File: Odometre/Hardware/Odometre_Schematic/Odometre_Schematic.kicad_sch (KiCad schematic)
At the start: 35 parts, among them IC1 STM32C092FCP6, J1 Conn_01x03_Pin, J2 Conn_01x03_Pin, J3 Conn_Alim, J4 Conn_Laser1, J5 Conn_Laser2, J6 Conn_01x06_Pin, J7 Conn_01x06_Pin, SW1 Reset_Botton, SW2 Debug_Botton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

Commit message: 5V
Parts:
- J7: footprint Connector_JST:JST_PH_B6B-PH-K_1x06_P2.00mm_Vertical -> Connector_PinHeader_2.54mm:PinHeader_1x03_P2.54mm_Vertical
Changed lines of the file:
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@@
+	)
+	(symbol
+		(lib_id "power:+5V")
+		(at 160.02 78.74 0)
+		(unit 1)
+		(exclude_from_sim no)
+		(in_bom yes)
+		(on_board yes)
+		(dnp no)
+		(fields_autoplaced yes)
+		(property "Reference" "#PWR09"
+			(at 160.02 82.55 0)
+			(effects
+				(font
+					(size 1.27 1.27)
+				)
+				(hide yes)
+			)
+		)
+		(property "Value" "+5V"
+			(at 160.02 73.66 0)
+			(effects
+				(font
+					(size 1.27 1.27)
+				)
+			)
+		)
+		(property "Footprint" ""
+			(at 160.02 78.74 0)
+			(effects
+				(font
+					(size 1.27 1.27)
+				)
+				(hide yes)
+			)
+		)
+		(property "Datasheet" ""
+			(at 160.02 78.74 0)
+			(effects
+				(font
+					(size 1.27 1.27)
+				)
+				(hide yes)
+			)
+		)
+		(property "Description" "Power symbol creates a global label with name \"+5V\""
+			(at 160.02 78.74 0)
+			(effects
+				(font
+					(size 1.27 1.27)
+				)
+				(hide yes)
+			)
+		)
+		(pin "1"
+		)
+		(instances
+			(project ""
+				(path "/3741a7b9-879e-49a1-88bd-82d63456a983"
+					(reference "#PWR09")
+					(unit 1)
+				)
+			)
+		)
 	)
 	(symbol
@@
 			)
 		)
-		(property "Footprint" "Connector_JST:JST_PH_B6B-PH-K_1x06_P2.00mm_Vertical"
+		(property "Footprint" "Connector_PinHeader_2.54mm:PinHeader_1x03_P2.54mm_Vertical"
 			(at 83.82 180.34 0)
 			(effects
@@
 					(unit 1)
 				)
-			)
-		)
-	)
-	(symbol
-		(lib_id "power:+5V")
-		(at 160.02 78.74 0)
-		(unit 1)
-		(exclude_from_sim no)
-		(in_bom yes)
-		(on_board yes)
-		(dnp no)
-		(fields_autoplaced yes)
-		(property "Reference" "#PWR09"
-			(at 160.02 82.55 0)
-			(effects
-				(font
-					(size 1.27 1.27)
-				)
-				(hide yes)
-			)
-		)
-		(property "Value" "+5V"
-			(at 160.02 73.66 0)
-			(effects
-				(font
-					(size 1.27 1.27)
-				)
-			)
-		)
-		(property "Footprint" ""
-			(at 160.02 78.74 0)
-			(effects
-				(font
-					(size 1.27 1.27)
-				)
-				(hide yes)
-			)
-		)
-		(property "Datasheet" ""
-			(at 160.02 78.74 0)
-			(effects
-				(font
-					(size 1.27 1.27)
-				)
-				(hide yes)
-			)
-		)
-		(property "Description" "Power symbol creates a global label with name \"+5V\""
-			(at 160.02 78.74 0)
-			(effects
-				(font
-					(size 1.27 1.27)
-				)
-				(hide yes)
-			)
-		)
-		(pin "1"
-		)
-		(instances
-			(project ""
-				(path "/3741a7b9-879e-49a1-88bd-82d63456a983"
-					(reference "#PWR09")
-					(unit 1)
-				)

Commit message: footprint modifiées
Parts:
- J1, J2: footprint Connector_PinHeader_2.54mm:PinHeader_1x03_P2.54mm_Vertical -> Connector_JST:JST_PH_B3B-PH-K_1x03_P2.00mm_Vertical
- J7: footprint Connector_PinHeader_2.54mm:PinHeader_1x03_P2.54mm_Vertical -> Connector_JST:JST_PH_B6B-PH-K_1x06_P2.00mm_Vertical
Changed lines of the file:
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@@
 			)
 		)
-		(property "Footprint" "Connector_PinHeader_2.54mm:PinHeader_1x03_P2.54mm_Vertical"
+		(property "Footprint" "Connector_JST:JST_PH_B3B-PH-K_1x03_P2.00mm_Vertical"
 			(at 99.06 149.86 0)
 			(effects
@@
 			)
 		)
-		(property "Footprint" "Connector_PinHeader_2.54mm:PinHeader_1x03_P2.54mm_Vertical"
+		(property "Footprint" "Connector_JST:JST_PH_B3B-PH-K_1x03_P2.00mm_Vertical"
 			(at 99.06 133.35 0)
 			(effects
@@
 			)
 		)
-		(property "Footprint" "Connector_PinHeader_2.54mm:PinHeader_1x03_P2.54mm_Vertical"
+		(property "Footprint" "Connector_JST:JST_PH_B6B-PH-K_1x06_P2.00mm_Vertical"
 			(at 83.82 180.34 0)
 			(effects

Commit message: import empreintes
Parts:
- removed SW1: Reset_Botton, Button_Switch_THT:SW_PUSH_6mm, symbol Switch:SW_Push
- removed SW2: Debug_Botton, Button_Switch_THT:SW_PUSH_6mm, symbol Switch:SW_Push
- added S1, S2: 430182043816, 430182043816:430182043816, symbol 430182043816:430182043816
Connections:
- net D_Botton: now also S2.1
- net GND: now also S1.4, S2.4
- net NRST: now also S1.1
- no-connect marks 11 -> 15

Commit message: import empreinte
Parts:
- S1, S2: footprint 430182043816:430182043816 -> projo:430182043816
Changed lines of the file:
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@@
 			)
 		)
-		(property "Footprint" "430182043816:430182043816"
+		(property "Footprint" "projo:430182043816"
 			(at 259.08 87.63 0)
 			(effects
@@
 			)
 		)
-		(property "Footprint" "430182043816:430182043816"
+		(property "Footprint" "projo:430182043816"
 			(at 259.08 109.22 0)
 			(effects

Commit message: modif empreintes
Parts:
- J4, J5: footprint Connector_PinSocket_2.54mm:PinSocket_1x02_P2.54mm_Vertical -> Connector_PinHeader_2.54mm:PinHeader_1x03_P2.54mm_Vertical
- J6: footprint Connector_PinHeader_2.54mm:PinHeader_1x03_P2.54mm_Vertical -> Connector_PinHeader_2.54mm:PinHeader_1x06_P2.54mm_Vertical
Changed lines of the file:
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@@
 			)
 		)
-		(property "Footprint" "Connector_PinSocket_2.54mm:PinSocket_1x02_P2.54mm_Vertical"
+		(property "Footprint" "Connector_PinHeader_2.54mm:PinHeader_1x03_P2.54mm_Vertical"
 			(at 36.83 172.72 0)
 			(effects
@@
 			)
 		)
-		(property "Footprint" "Connector_PinSocket_2.54mm:PinSocket_1x02_P2.54mm_Vertical"
+		(property "Footprint" "Connector_PinHeader_2.54mm:PinHeader_1x03_P2.54mm_Vertical"
 			(at 36.83 185.42 0)
 			(effects
@@
 			)
 		)
-		(property "Footprint" "Connector_PinHeader_2.54mm:PinHeader_1x03_P2.54mm_Vertical"
+		(property "Footprint" "Connector_PinHeader_2.54mm:PinHeader_1x06_P2.54mm_Vertical"
 			(at 39.37 137.16 0)
 			(effects

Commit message: modifs che pas
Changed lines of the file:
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@@
 	)
 	(junction
+		(at 120.65 31.75)
+		(diameter 0)
+		(color 0 0 0 0)
+	)
+	(junction
 		(at 120.65 78.74)
 		(diameter 0)
@@
 	)
 	(junction
-		(at 120.65 31.75)
+		(at 128.27 31.75)
 		(diameter 0)
 		(color 0 0 0 0)
@@
 	(wire
 		(pts
+			(xy 128.27 31.75) (xy 133.35 31.75)
+		)
+		(stroke
+			(width 0)
+			(type default)
+		)
+	)
+	(wire
+		(pts
 			(xy 74.93 78.74) (xy 74.93 81.28)
 		)
@@
 	(wire
 		(pts
-			(xy 120.65 31.75) (xy 133.35 31.75)
-		)
-		(stroke
-			(width 0)
-			(type default)
-		)
-	)
-	(wire
-		(pts
 			(xy 261.62 93.98) (xy 270.51 93.98)
 		)
@@
 	(wire
 		(pts
+			(xy 120.65 31.75) (xy 128.27 31.75)
+		)
+		(stroke
+			(width 0)
+			(type default)
+		)
+	)
+	(wire
+		(pts
 			(xy 252.73 54.61) (xy 256.54 54.61)
 		)
@@
 					(unit 1)
 				)
+			)
+		)
+	)
+	(symbol
+		(lib_id "power:PWR_FLAG")
+		(at 128.27 31.75 0)
+		(unit 1)
+		(exclude_from_sim no)
+		(in_bom yes)
+		(on_board yes)
+		(dnp no)
+		(fields_autoplaced yes)
+		(property "Reference" "#FLG01"
+			(at 128.27 29.845 0)
+			(effects
+				(font
+					(size 1.27 1.27)
+				)
+				(hide yes)
+			)
+		)
+		(property "Value" "PWR_FLAG"
+			(at 128.27 26.67 0)
+			(effects
+				(font
+					(size 1.27 1.27)
+				)
+			)
+		)
+		(property "Footprint" ""
+			(at 128.27 31.75 0)
+			(effects
+				(font
+					(size 1.27 1.27)
+				)
+				(hide yes)
+			)
+		)
+		(property "Datasheet" "~"
+			(at 128.27 31.75 0)
+			(effects
+				(font
+					(size 1.27 1.27)
+				)
+				(hide yes)
+			)
+		)
+		(property "Description" "Special symbol for telling ERC where power comes from"
+			(at 128.27 31.75 0)
+			(effects
+				(font
+					(size 1.27 1.27)
+				)
+				(hide yes)
+			)
+		)
+		(pin "1"
+		)
+		(instances
+			(project ""
+				(path "/3741a7b9-879e-49a1-88bd-82d63456a983"
+					(reference "#FLG01")
+					(unit 1)
+				)

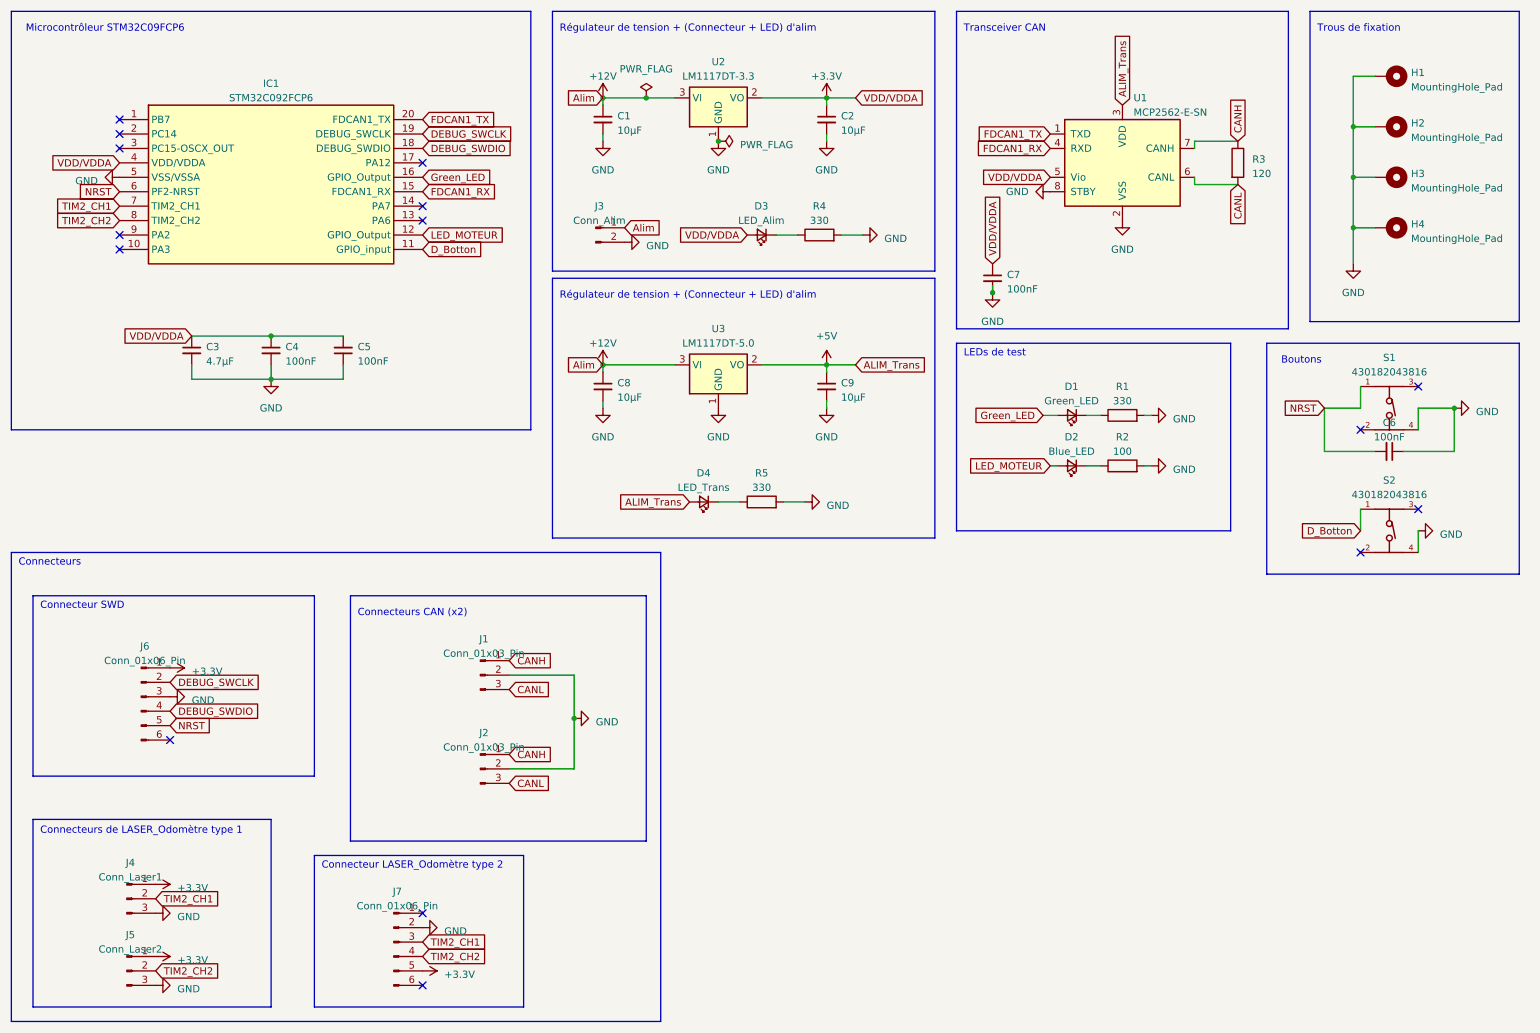
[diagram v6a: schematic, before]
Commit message: routage du pcb
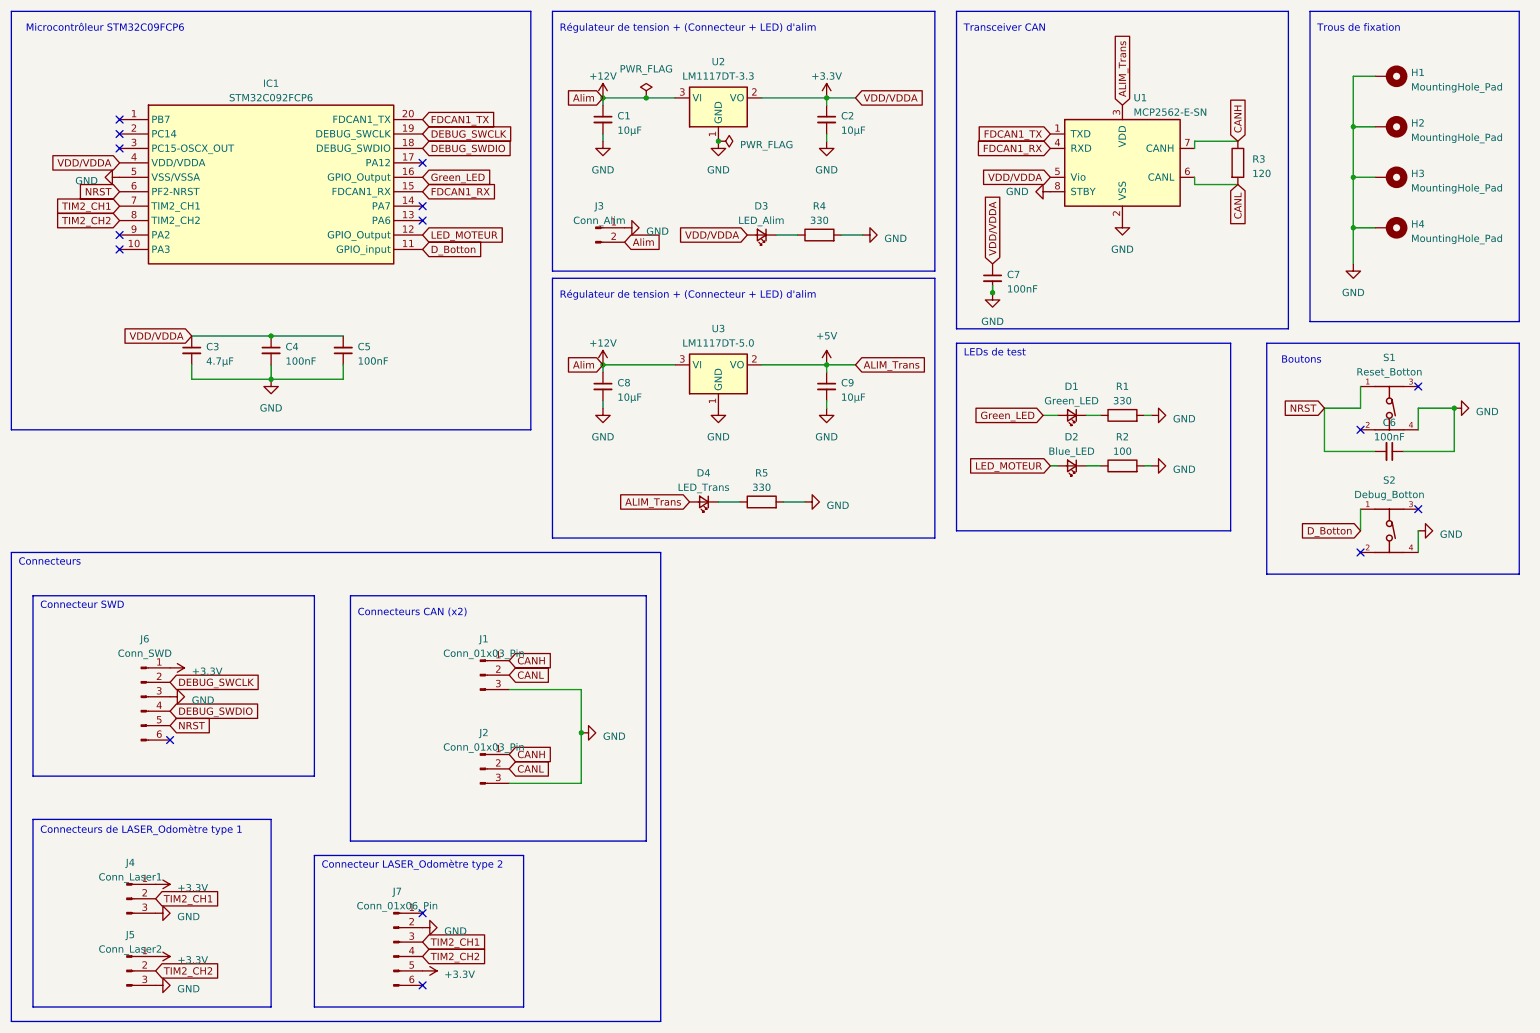
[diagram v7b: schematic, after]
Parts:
- J6: value Conn_01x06_Pin -> Conn_SWD
- S1: value 430182043816 -> Reset_Botton
- S2: value 430182043816 -> Debug_Botton
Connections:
- net +12V: now also J3.2 (Pin_2); no longer J3.1 (Pin_1)
- net CANL: now also J1.2 (Pin_2), J2.2 (Pin_2); no longer J1.3 (Pin_3), J2.3 (Pin_3)
- net GND: now also J1.3 (Pin_3), J2.3 (Pin_3), J3.1 (Pin_1); no longer J1.2 (Pin_2), J2.2 (Pin_2), J3.2 (Pin_2)
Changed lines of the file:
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@@
 	)
 	(junction
-		(at 115.57 140.97)
+		(at 116.84 143.51)
 		(diameter 0)
 		(color 0 0 0 0)
@@
 	(wire
 		(pts
-			(xy 115.57 149.86) (xy 104.14 149.86)
-		)
-		(stroke
-			(width 0)
-			(type default)
-		)
-	)
-	(wire
-		(pts
 			(xy 256.54 27.94) (xy 252.73 27.94)
 		)
@@
 	(wire
 		(pts
-			(xy 115.57 140.97) (xy 115.57 149.86)
+			(xy 116.84 143.51) (xy 116.84 152.4)
 		)
 		(stroke
@@
 	(wire
 		(pts
+			(xy 104.14 135.89) (xy 116.84 135.89)
+		)
+		(stroke
+			(width 0)
+			(type default)
+		)
+	)
+	(wire
+		(pts
 			(xy 120.65 31.75) (xy 120.65 33.02)
 		)
@@
 	(wire
 		(pts
+			(xy 104.14 152.4) (xy 116.84 152.4)
+		)
+		(stroke
+			(width 0)
+			(type default)
+		)
+	)
+	(wire
+		(pts
 			(xy 160.02 86.36) (xy 160.02 85.09)
 		)
@@
 	(wire
 		(pts
-			(xy 115.57 133.35) (xy 115.57 140.97)
+			(xy 116.84 135.89) (xy 116.84 143.51)
 		)
 		(stroke
@@
 	(wire
 		(pts
-			(xy 104.14 133.35) (xy 115.57 133.35)
-		)
-		(stroke
-			(width 0)
-			(type default)
-		)
-	)
-	(wire
-		(pts
 			(xy 162.56 55.88) (xy 166.37 55.88)
 		)
@@
 	(global_label "Alim"
 		(shape input)
-		(at 124.46 54.61 0)
+		(at 124.46 57.15 0)
 		(fields_autoplaced yes)
 		(effects
@@
 		)
 		(property "Intersheetrefs" "${INTERSHEET_REFS}"
-			(at 131.4177 54.61 0)
+			(at 131.4177 57.15 0)
 			(effects
 				(font
@@
 	(global_label "CANL"
 		(shape input)
-		(at 104.14 152.4 0)
+		(at 104.14 149.86 0)
 		(fields_autoplaced yes)
 		(effects
@@
 		)
 		(property "Intersheetrefs" "${INTERSHEET_REFS}"
-			(at 111.763 152.4 0)
+			(at 111.763 149.86 0)
 			(effects
 				(font
@@
 	(global_label "CANL"
 		(shape input)
-		(at 104.14 135.89 0)
+		(at 104.14 133.35 0)
 		(fields_autoplaced yes)
 		(effects
@@
 		)
 		(property "Intersheetrefs" "${INTERSHEET_REFS}"
-			(at 111.763 135.89 0)
+			(at 111.763 133.35 0)
 			(effects
 				(font
@@
 			)
 		)
-		(property "Value" "430182043816"
+		(property "Value" "Reset_Botton"
 			(at 259.08 80.01 0)
 			(effects
@@
 			)
 		)
-		(property "Value" "430182043816"
+		(property "Value" "Debug_Botton"
 			(at 259.08 101.6 0)
 			(effects
@@
 	(symbol
 		(lib_id "power:GND")
-		(at 115.57 140.97 90)
+		(at 116.84 143.51 90)
 		(unit 1)
 		(exclude_from_sim no)
@@
 		(fields_autoplaced yes)
 		(property "Reference" "#PWR022"
-			(at 121.92 140.97 0)
+			(at 123.19 143.51 0)
 			(effects
 				(font
@@
 		)
 		(property "Value" "GND"
-			(at 119.38 141.605 90)
+			(at 120.65 144.145 90)
 			(effects
 				(font
@@
 		)
 		(property "Footprint" ""
-			(at 115.57 140.97 0)
+			(at 116.84 143.51 0)
 			(effects
 				(font
@@
 		)
 		(property "Datasheet" ""
-			(at 115.57 140.97 0)
+			(at 116.84 143.51 0)
 			(effects
 				(font
@@
 		)
 		(property "Description" ""
-			(at 115.57 140.97 0)
+			(at 116.84 143.51 0)
 			(effects
 				(font
@@
 	(symbol
 		(lib_id "power:GND")
-		(at 124.46 57.15 90)
+		(at 124.46 54.61 90)
 		(unit 1)
 		(exclude_from_sim no)
@@
 		(fields_autoplaced yes)
 		(property "Reference" "#PWR019"
-			(at 130.81 57.15 0)
+			(at 130.81 54.61 0)
 			(effects
 				(font
@@
 		)
 		(property "Value" "GND"
-			(at 128.27 57.785 90)
+			(at 128.27 55.245 90)
 			(effects
 				(font
@@
 		)
 		(property "Footprint" ""
-			(at 124.46 57.15 0)
+			(at 124.46 54.61 0)
 			(effects
 				(font
@@
 		)
 		(property "Datasheet" ""
-			(at 124.46 57.15 0)
+			(at 124.46 54.61 0)
 			(effects
 				(font
@@
 		)
 		(property "Description" ""
-			(at 124.46 57.15 0)
+			(at 124.46 54.61 0)
 			(effects
 				(font
@@
 		(fields_autoplaced yes)
 		(property "Reference" "J6"
-			(at 40.005 128.27 0)
+			(at 40.005 127 0)
 			(effects
 				(font
@@
 			)
 		)
-		(property "Value" "Conn_01x06_Pin"
-			(at 40.005 130.81 0)
+		(property "Value" "Conn_SWD"
+			(at 40.005 129.54 0)
 			(effects
 				(font

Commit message: modif d'empreintes
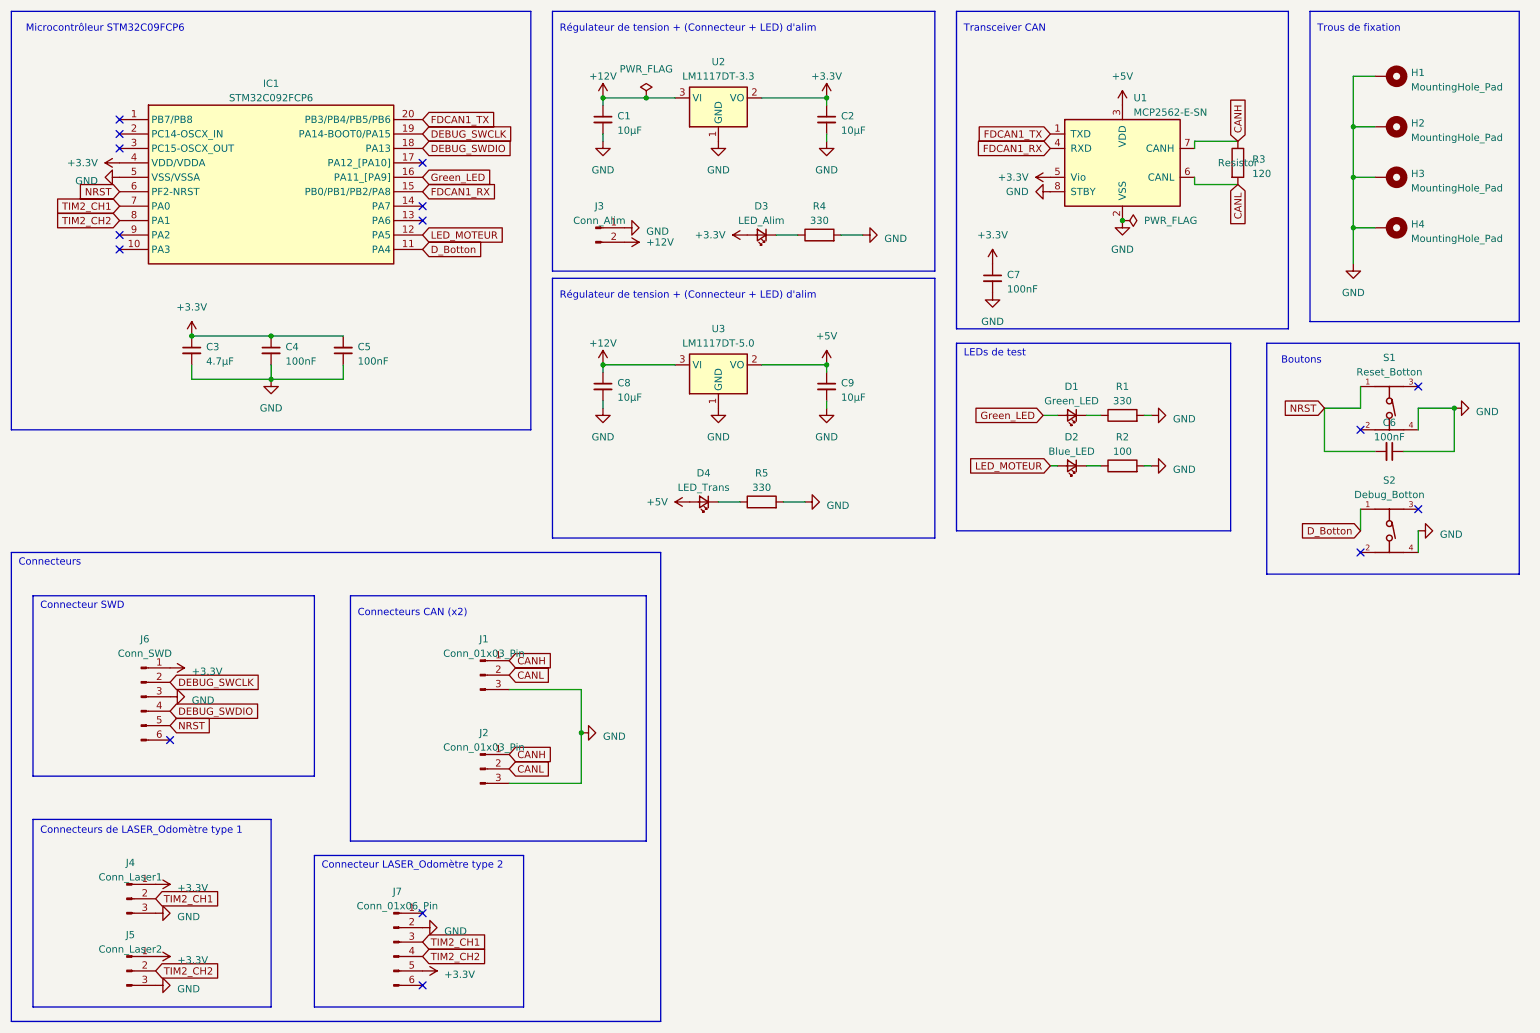
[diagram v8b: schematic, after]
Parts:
- IC1: footprint Package_SO:TSSOP-20_4.4x6.5mm_P0.65mm -> projo:SOP65P640X120-20N
